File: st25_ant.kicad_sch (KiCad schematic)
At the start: 0 parts

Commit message: added ST25DV64KC-IE6T3
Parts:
- added U1: ST25DV64KC-IE6T3, symbol symbols:ST25DV64KC-IE6T3
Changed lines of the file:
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@@
 	(generator_version "10.0")
 	(paper "A4")
+	(symbol
+		(lib_id "symbols:ST25DV64KC-IE6T3")
+		(at 144.78 93.98 0)
+		(unit 1)
+		(body_style 1)
+		(exclude_from_sim no)
+		(in_bom yes)
+		(on_board yes)
+		(in_pos_files yes)
+		(dnp no)
+		(property "Reference" "U1"
+			(at 153.67 80.264 0)
+			(show_name no)
+			(do_not_autoplace no)
+			(effects
+				(font
+					(size 1.27 1.27)
+				)
+			)
+		)
+		(property "Value" "ST25DV64KC-IE6T3"
+			(at 143.764 107.95 0)
+			(show_name no)
+			(do_not_autoplace no)
+			(effects
+				(font
+					(size 1.27 1.27)
+				)
+			)
+		)
+		(property "Footprint" ""
+			(at 144.78 93.98 0)
+			(hide yes)
+			(show_name no)
+			(do_not_autoplace no)
+			(effects
+				(font
+					(size 1.27 1.27)
+				)
+			)
+		)
+		(property "Datasheet" "file:///home/atta/Documents/kicad/AetherInk/datasheets/ST25DV64KC/st25dv04kc.pdf"
+			(at 144.78 93.98 0)
+			(hide yes)
+			(show_name no)
+			(do_not_autoplace no)
+			(effects
+				(font
+					(size 1.27 1.27)
+				)
+			)
+		)
+		(property "Description" "ynamic NFC/RFID tag IC with 4-, 16-, or 64-Kbit EEPROM, fast transfer mode capability, and optimized I2C"
+			(at 144.78 93.98 0)
+			(hide yes)
+			(show_name no)
+			(do_not_autoplace no)
+			(effects
+				(font
+					(size 1.27 1.27)
+				)
+			)
+		)
+		(pin "8"
+		)
+		(pin "7"
+		)
+		(pin "3"
+		)
+		(pin "1"
+		)
+		(pin "6"
+		)
+		(pin "5"
+		)
+		(pin "2"
+		)
+		(pin "4"
+		)
+		(instances
+			(project "AetherInk"
+				(path "/bfe982fc-ac83-4361-b0ed-d42b62c23a78/98cf7c84-db45-46dc-975b-3c91e5d6f6fa"
+					(reference "U1")
+					(unit 1)
+				)
+			)
+		)
+	)
 )

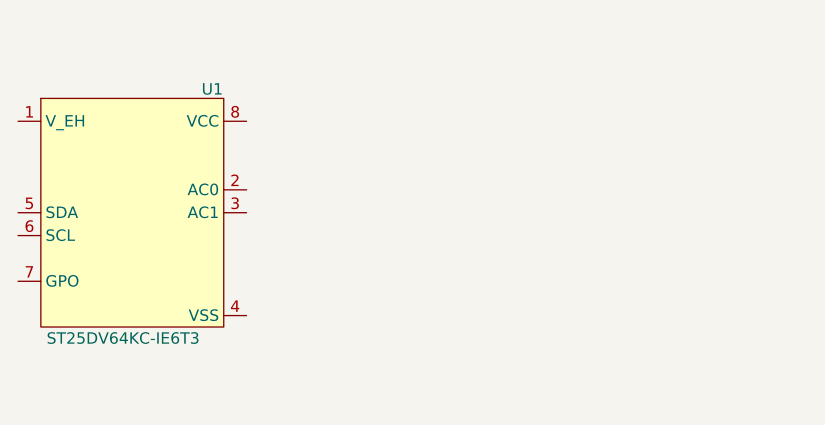
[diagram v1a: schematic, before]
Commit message: most of st25 is now done, only the power selection is remaning
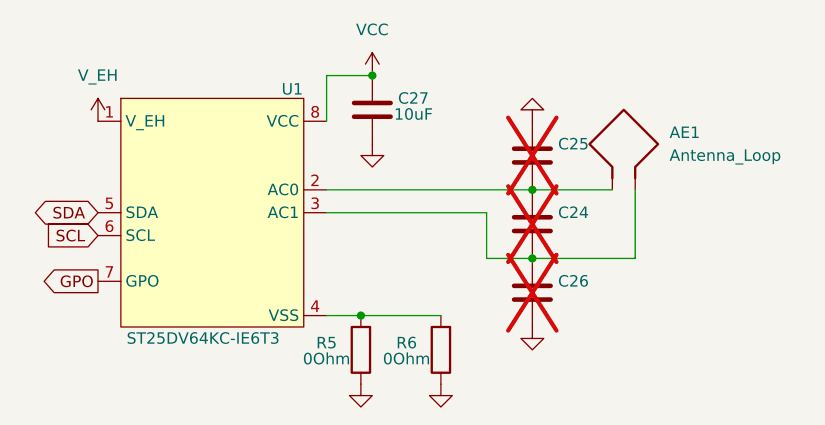
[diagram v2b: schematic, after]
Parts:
- added AE1: Antenna_Loop, symbol Device:Antenna_Loop
- added C24, C25, C26: (no value), symbol Device:C
- added C27: 10uF, symbol Device:C
- added R5, R6: 0Ohm, symbol Device:R
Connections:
- net V_EH: now reaches U1.1 (V_EH)
- net at U1.2 (AC0): now also AE1.1, C24.2, C25.1
- net at U1.3 (AC1): now also AE1.2, C24.1, C26.2
- net at U1.4 (VSS): now also R5.2, R6.2
- net SDA: now reaches U1.5 (SDA)
- net SCL: now reaches U1.6 (SCL)
- net GPO: now reaches U1.7 (GPO)
- net VCC: now reaches U1.8 (VCC)
- net VCC: now also C27.2
- new net GND: C25.2, C26.1, C27.1, R5.1, R6.1

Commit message: done the st25
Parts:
- added C28: 4.7uF/25V, symbol Device:C
- added C29: 100nF, symbol Device:C
- added C30: 10nF, symbol Device:C
- added C31: (no value), symbol Device:C
- added J2: Conn_01x02, symbol Connector_Generic:Conn_01x02
- added J3: Conn_01x03, symbol Connector_Generic:Conn_01x03
- added R7: 0Ohm, symbol Device:R
- C27: value 10uF -> 10nF
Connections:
- net GND: now also C28.1, C29.1, C30.1, C31.1
- net VCC: now also C28.2, C29.2, J3.2 (Pin_2)
- net V_EH: now also C30.2, R7.2
- new net +3V3: J2.1 (Pin_1), J3.1 (Pin_1)
- new net EH: C31.2, J2.2 (Pin_2), J3.3 (Pin_3), R7.1
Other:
- moved on the sheet: AE1, C24, C25, C26, C27, R5, R6, U1
